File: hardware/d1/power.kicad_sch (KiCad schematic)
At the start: 0 parts

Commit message: New components
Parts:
- added U7: TPS7A2018PDBVR, JLCImport:TPS7A2018PDBVR, symbol JLCImport:TPS7A2018PDBVR
- added U8: TPS7A2033PDBVR, JLCImport:TPS7A2033PDBVR, symbol JLCImport:TPS7A2033PDBVR
- added U9: TPS560430XFDBVR, JLCImport:TPS560430XFDBVR, symbol JLCImport:TPS560430XFDBVR
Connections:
- new net +3V8: U8.1 (IN)
- new net GND: U8.2 (GND)
- no-connect marks 0 -> 1

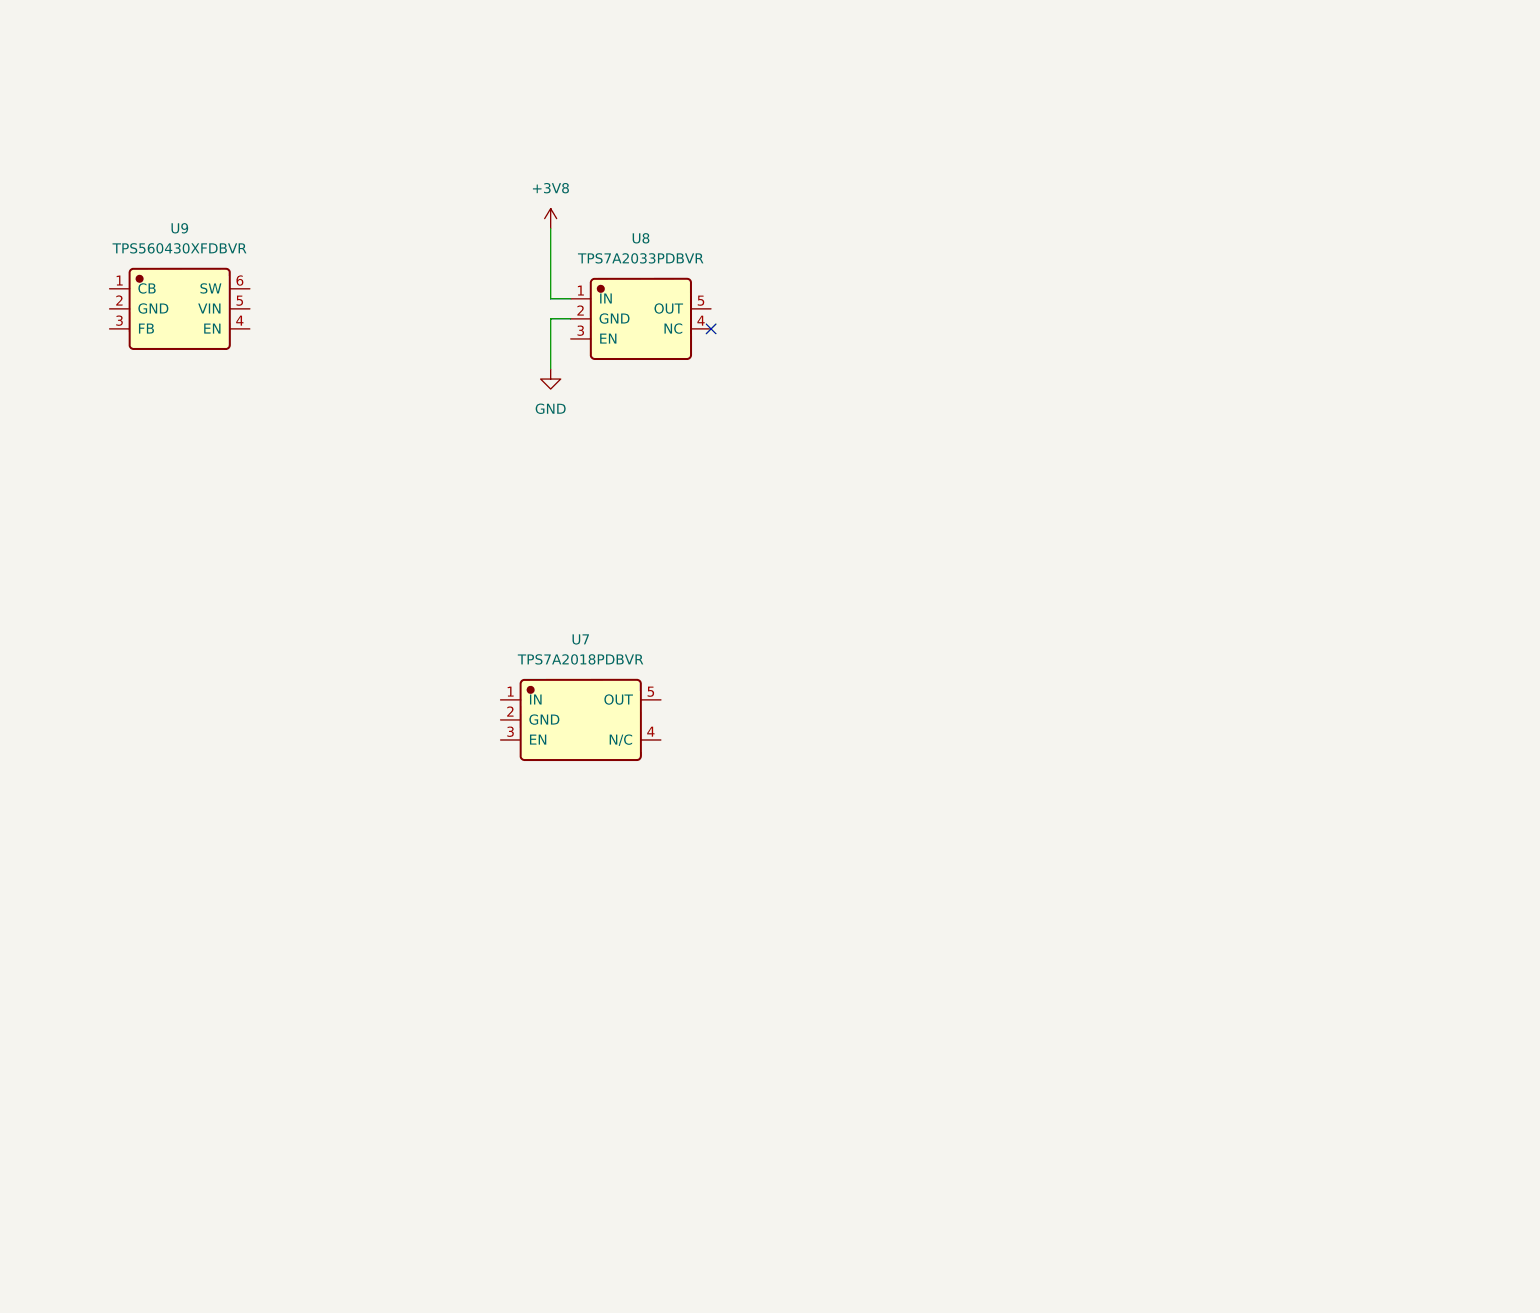
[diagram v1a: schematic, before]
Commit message: Change uart pins, add components
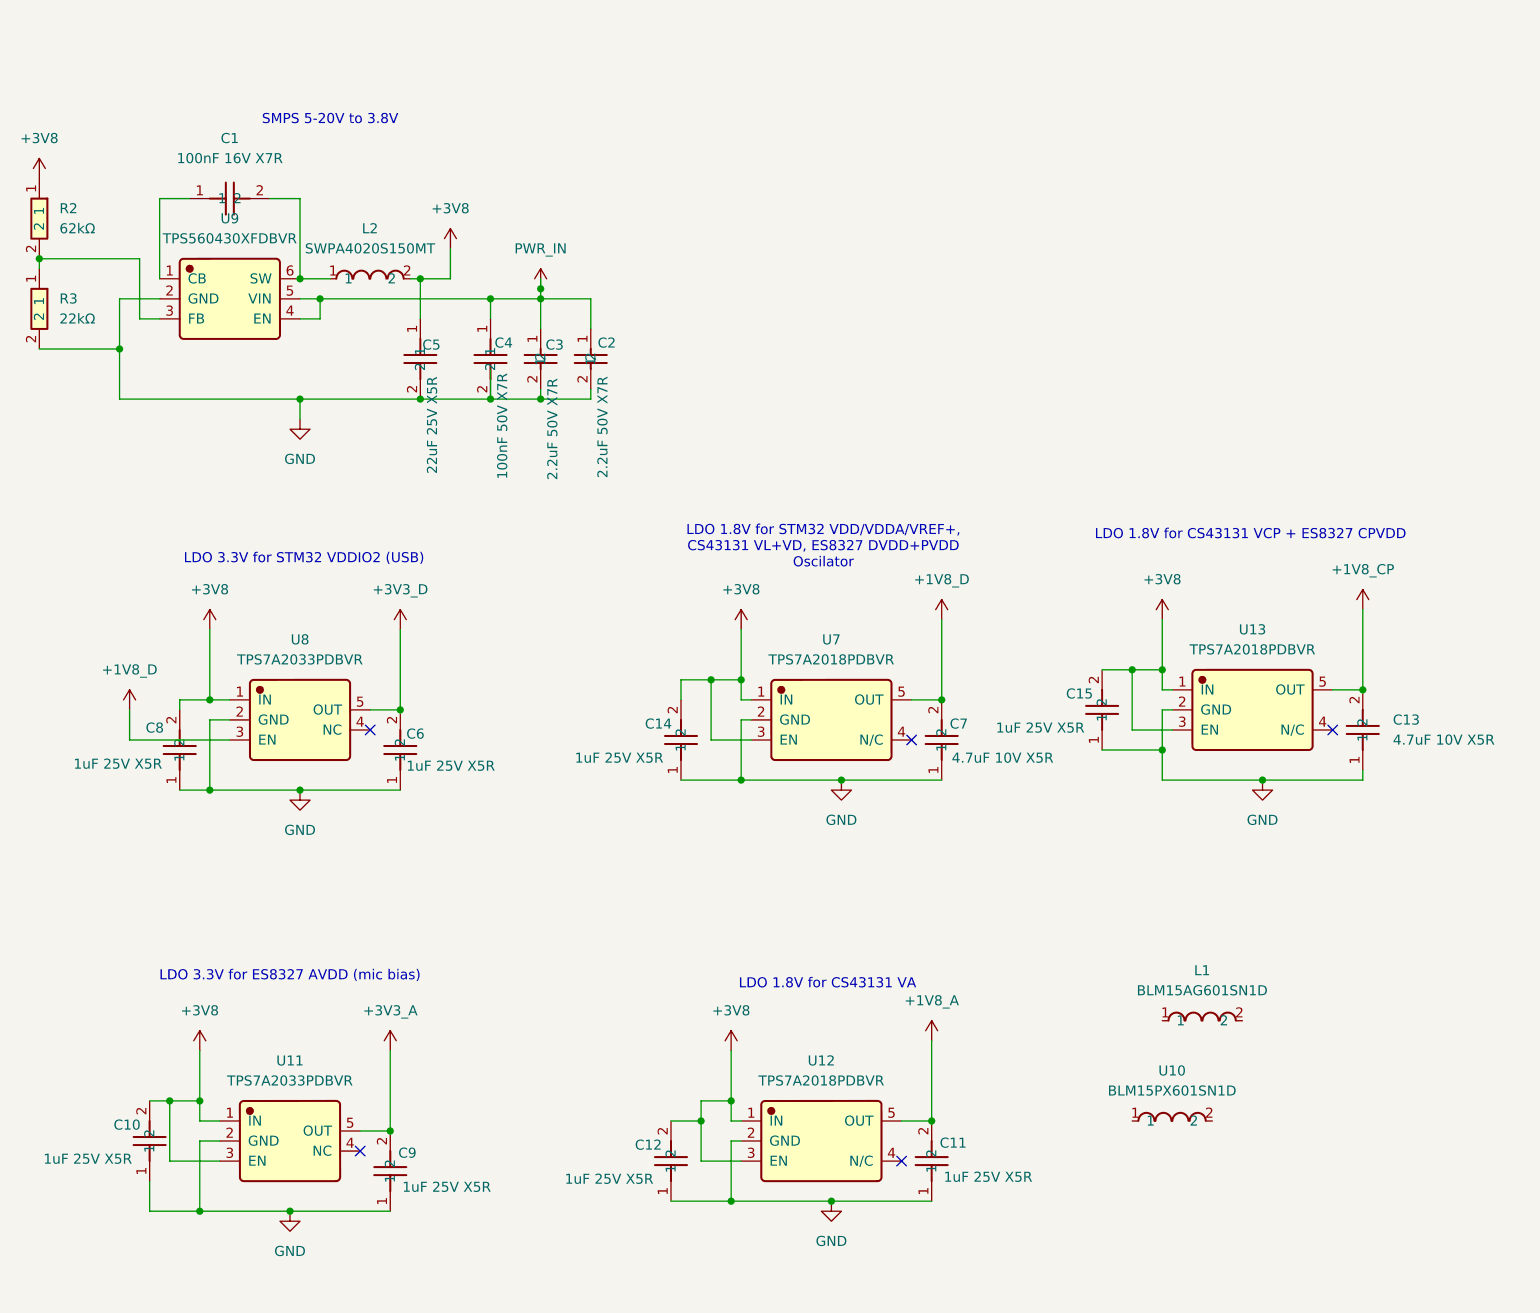
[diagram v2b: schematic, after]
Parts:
- added C1: 100nF 16V X7R, JLCImport:CL05B104KO5NNNC, symbol JLCImport:CL05B104KO5NNNC
- added C10, C11, C12, C14, C15, C6, C8, C9: 1uF 25V X5R, JLCImport:CL05A105KA5NQNC, symbol JLCImport:CL05A105KA5NQNC
- added C13, C7: 4.7uF 10V X5R, JLCImport:CL05A475MP5NRNC, symbol JLCImport:CL05A475MP5NRNC
- added C2, C3: 2.2uF 50V X7R, JLCImport:CC0805KKX7R9BB225, symbol JLCImport:CC0805KKX7R9BB225
- added C4: 100nF 50V X7R, JLCImport:CL05B104KB54PNC, symbol JLCImport:CL05B104KB54PNC
- added C5: 22uF 25V X5R, JLCImport:CL21A226MAQNNNE, symbol JLCImport:CL21A226MAQNNNE
- added L1: BLM15AG601SN1D, JLCImport:BLM15AG601SN1D, symbol JLCImport:BLM15AG601SN1D
- added L2: SWPA4020S150MT, JLCImport:SWPA4020S150MT, symbol JLCImport:SWPA4020S150MT
- added R2: 62kΩ, JLCImport:0402WGF6202TCE, symbol JLCImport:0402WGF6202TCE
- added R3: 22kΩ, JLCImport:0402WGF2202TCE, symbol JLCImport:0402WGF2202TCE
- added U10: BLM15PX601SN1D, JLCImport:BLM15PX601SN1D, symbol JLCImport:BLM15PX601SN1D
- added U11: TPS7A2033PDBVR, JLCImport:TPS7A2033PDBVR, symbol JLCImport:TPS7A2033PDBVR
- added U12, U13: TPS7A2018PDBVR, JLCImport:TPS7A2018PDBVR, symbol JLCImport:TPS7A2018PDBVR
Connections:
- net +3V8: now also U7.1 (IN), U7.3 (EN), C10.2, C12.2, C14.2, C15.2, C5.1, C8.2, L2.2, R2.1, U11.1 (IN), U11.3 (EN), U12.1 (IN), U12.3 (EN), U13.1 (IN), U13.3 (EN)
- net GND: now also U7.2 (GND), U9.2 (GND), C10.1, C11.1, C12.1, C13.1, C14.1, C15.1, C2.2, C3.2, C4.2, C5.2, C6.1, C7.1, C8.1, C9.1, R3.2, U11.2 (GND), U12.2 (GND), U13.2 (GND)
- net +1V8_D: now reaches U8.3 (EN)
- net +1V8_D: now also U7.5 (OUT), C7.2
- net +3V3_D: now reaches U8.5 (OUT)
- net +3V3_D: now also C6.2
- net at U9.1 (CB): now also C1.1
- net at U9.3 (FB): now also R2.2, R3.1
- net PWR_IN: now reaches U9.4 (EN)
- net PWR_IN: now also U9.5 (VIN), C2.1, C3.1, C4.1
- net at U9.6 (SW): now also C1.2, L2.1
- new net +1V8_A: C11.2, U12.5 (OUT)
- new net +1V8_CP: C13.2, U13.5 (OUT)
- new net +3V3_A: C9.2, U11.5 (OUT)
- no-connect marks 1 -> 5
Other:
- note added: "LDO 1.8V for CS43131 VA"
- note added: "LDO 1.8V for CS43131 VCP + ES8327 CPVDD"
- note added: "LDO 1.8V for STM32 VDD/VDDA/VREF+, CS43131 VL+VD, ES8327 DVDD+PVDD Oscilator"
- note added: "LDO 3.3V for ES8327 AVDD (mic bias)"
- note added: "LDO 3.3V for STM32 VDDIO2 (USB)"
- note added: "SMPS 5-20V to 3.8V"
- moved on the sheet: U7, U8, U9

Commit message: Add new parts
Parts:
- removed L1: BLM15AG601SN1D, JLCImport:BLM15AG601SN1D, symbol JLCImport:BLM15AG601SN1D
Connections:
- net +3V8: now also U10.1; no longer C12.2, U12.1 (IN), U12.3 (EN)
- net at U10.2: now also C12.2, U12.1 (IN), U12.3 (EN)
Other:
- moved on the sheet: U10
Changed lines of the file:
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@@
 	)
 	(junction
-		(at 111.76 152.4)
-		(diameter 0)
-		(color 0 0 0 0)
-	)
-	(junction
 		(at 166.37 97.79)
 		(diameter 0)
@@
 	)
 	(junction
+		(at 111.76 152.4)
+		(diameter 0)
+		(color 0 0 0 0)
+	)
+	(junction
 		(at 113.03 111.76)
 		(diameter 0)
@@
 	(wire
 		(pts
+			(xy 91.44 146.05) (xy 99.06 146.05)
+		)
+		(stroke
+			(width 0)
+			(type default)
+		)
+	)
+	(wire
+		(pts
 			(xy 111.76 165.1) (xy 137.16 165.1)
 		)
@@
 	(wire
 		(pts
+			(xy 109.22 146.05) (xy 111.76 146.05)
+		)
+		(stroke
+			(width 0)
+			(type default)
+		)
+	)
+	(wire
+		(pts
 			(xy 111.76 154.94) (xy 113.03 154.94)
 		)
@@
 	(wire
 		(pts
-			(xy 111.76 146.05) (xy 111.76 152.4)
-		)
-		(stroke
-			(width 0)
-			(type default)
-		)
-	)
-	(wire
-		(pts
 			(xy 137.16 154.94) (xy 133.35 154.94)
 		)
@@
 	(wire
 		(pts
+			(xy 111.76 146.05) (xy 111.76 152.4)
+		)
+		(stroke
+			(width 0)
+			(type default)
+		)
+	)
+	(wire
+		(pts
 			(xy 111.76 152.4) (xy 111.76 154.94)
 		)
@@
 	)
 	(symbol
+		(lib_id "power:+3V8")
+		(at 91.44 146.05 0)
+		(unit 1)
+		(body_style 1)
+		(exclude_from_sim no)
+		(in_bom yes)
+		(on_board yes)
+		(in_pos_files yes)
+		(dnp no)
+		(fields_autoplaced yes)
+		(property "Reference" "#PWR011"
+			(at 91.44 149.86 0)
+			(hide yes)
+			(show_name no)
+			(do_not_autoplace no)
+			(effects
+				(font
+					(size 1.27 1.27)
+				)
+			)
+		)
+		(property "Value" "+3V8"
+			(at 91.44 140.97 0)
+			(show_name no)
+			(do_not_autoplace no)
+			(effects
+				(font
+					(size 1.27 1.27)
+				)
+			)
+		)
+		(property "Footprint" ""
+			(at 91.44 146.05 0)
+			(hide yes)
+			(show_name no)
+			(do_not_autoplace no)
+			(effects
+				(font
+					(size 1.27 1.27)
+				)
+			)
+		)
+		(property "Datasheet" ""
+			(at 91.44 146.05 0)
+			(hide yes)
+			(show_name no)
+			(do_not_autoplace no)
+			(effects
+				(font
+					(size 1.27 1.27)
+				)
+			)
+		)
+		(property "Description" "Power symbol creates a global label with name \"+3V8\""
+			(at 91.44 146.05 0)
+			(hide yes)
+			(show_name no)
+			(do_not_autoplace no)
+			(effects
+				(font
+					(size 1.27 1.27)
+				)
+			)
+		)
+		(pin "1"
+		)
+		(instances
+			(project "DrunkEarPhoneAdapter"
+				(path "/df940915-8af0-46f9-b18a-23d4684ae671/bea21a31-aee1-46f9-b13e-ece764487360"
+					(reference "#PWR011")
+					(unit 1)
+				)
+			)
+		)
+	)
+	(symbol
 		(lib_id "power:+5V")
 		(at 87.63 49.53 0)
@@
 	(symbol
 		(lib_id "JLCImport:BLM15PX601SN1D")
-		(at 167.64 154.94 0)
+		(at 104.14 146.05 0)
 		(unit 1)
 		(body_style 1)
@@
 		(fields_autoplaced yes)
 		(property "Reference" "U10"
-			(at 167.6123 148.59 0)
+			(at 104.1123 139.7 0)
 			(show_name no)
 			(do_not_autoplace no)
@@
 		)
 		(property "Value" "BLM15PX601SN1D"
-			(at 167.6123 151.13 0)
+			(at 104.1123 142.24 0)
 			(show_name no)
 			(do_not_autoplace no)
@@
 		)
 		(property "Footprint" "JLCImport:BLM15PX601SN1D"
-			(at 167.64 154.94 0)
+			(at 104.14 146.05 0)
 			(hide yes)
 			(show_name no)
@@
 		)
 		(property "Datasheet" "https://www.lcsc.com/datasheet/lcsc_datasheet_2304140030_Murata-Electronics-BLM15PX601SN1D_C160977.pdf"
-			(at 167.64 154.94 0)
+			(at 104.14 146.05 0)
 			(hide yes)
 			(show_name no)
@@
 		)
 		(property "Description" "-55℃~+125℃ 1 230mΩ 600Ω@100MHz 900mA ±25% 0402 Ferrite Beads ROHS"
-			(at 167.64 154.94 0)
+			(at 104.14 146.05 0)
 			(hide yes)
 			(show_name no)
@@
 		)
 		(property "LCSC" "C160977"
-			(at 167.64 154.94 0)
+			(at 104.14 146.05 0)
 			(hide yes)
 			(show_name no)
@@
 		)
 		(property "Manufacturer" "Murata Electronics"
-			(at 167.64 154.94 0)
+			(at 104.14 146.05 0)
 			(hide yes)
 			(show_name no)
@@
 		)
 		(property "Manufacturer Part" "BLM15PX601SN1D"
-			(at 167.64 154.94 0)
+			(at 104.14 146.05 0)
 			(hide yes)
 			(show_name no)
@@
 	)
 	(symbol
-		(lib_id "power:+3V8")
-		(at 111.76 146.05 0)
-		(unit 1)
-		(body_style 1)
-		(exclude_from_sim no)
-		(in_bom yes)
-		(on_board yes)
-		(in_pos_files yes)
-		(dnp no)
-		(fields_autoplaced yes)
-		(property "Reference" "#PWR011"
-			(at 111.76 149.86 0)
-			(hide yes)
-			(show_name no)
-			(do_not_autoplace no)
-			(effects
-				(font
-					(size 1.27 1.27)
-				)
-			)
-		)
-		(property "Value" "+3V8"
-			(at 111.76 140.97 0)
-			(show_name no)
-			(do_not_autoplace no)
-			(effects
-				(font
-					(size 1.27 1.27)
-				)
-			)
-		)
-		(property "Footprint" ""
-			(at 111.76 146.05 0)
-			(hide yes)
-			(show_name no)
-			(do_not_autoplace no)
-			(effects
-				(font
-					(size 1.27 1.27)
-				)
-			)
-		)
-		(property "Datasheet" ""
-			(at 111.76 146.05 0)
-			(hide yes)
-			(show_name no)
-			(do_not_autoplace no)
-			(effects
-				(font
-					(size 1.27 1.27)
-				)
-			)
-		)
-		(property "Description" "Power symbol creates a global label with name \"+3V8\""
-			(at 111.76 146.05 0)
-			(hide yes)
-			(show_name no)
-			(do_not_autoplace no)
-			(effects
-				(font
-					(size 1.27 1.27)
-				)
-			)
-		)
-		(pin "1"
-		)
-		(instances
-			(project "DrunkEarPhoneAdapter"
-				(path "/df940915-8af0-46f9-b18a-23d4684ae671/bea21a31-aee1-46f9-b13e-ece764487360"
-					(reference "#PWR011")
-					(unit 1)
-				)
-			)
-		)
-	)
-	(symbol
 		(lib_id "JLCImport:TPS560430XFDBVR")
 		(at 48.26 50.8 0)
@@
 					(unit 1)
 				)
-			)
-		)
-	)
-	(symbol
-		(lib_id "JLCImport:BLM15AG601SN1D")
-		(at 171.45 142.24 0)
-		(unit 1)
-		(body_style 1)
-		(exclude_from_sim no)
-		(in_bom yes)
-		(on_board yes)
-		(in_pos_files yes)
-		(dnp no)
-		(fields_autoplaced yes)
-		(property "Reference" "L1"
-			(at 171.4233 135.89 0)
-			(show_name no)
-			(do_not_autoplace no)
-			(effects
-				(font
-					(size 1.27 1.27)
-				)
-			)
-		)
-		(property "Value" "BLM15AG601SN1D"
-			(at 171.4233 138.43 0)
-			(show_name no)
-			(do_not_autoplace no)
-			(effects
-				(font
-					(size 1.27 1.27)
-				)
-			)
-		)
-		(property "Footprint" "JLCImport:BLM15AG601SN1D"
-			(at 171.45 142.24 0)
-			(hide yes)
-			(show_name no)
-			(do_not_autoplace no)
-			(effects
-				(font
-					(size 1.27 1.27)
-				)
-			)
-		)
-		(property "Datasheet" "https://www.lcsc.com/datasheet/lcsc_datasheet_2304140030_Murata-Electronics-BLM15AG601SN1D_C76884.pdf"
-			(at 171.45 142.24 0)
-			(hide yes)
-			(show_name no)
-			(do_not_autoplace no)
-			(effects
-				(font
-					(size 1.27 1.27)
-				)
-			)
-		)
-		(property "Description" "-55℃~+125℃ 1 300mA 520mΩ 600Ω@100MHz ±25% 0402 Ferrite Beads ROHS"
-			(at 171.45 142.24 0)
-			(hide yes)
-			(show_name no)
-			(do_not_autoplace no)
-			(effects
-				(font
-					(size 1.27 1.27)
-				)
-			)
-		)
-		(property "LCSC" "C76884"
-			(at 171.45 142.24 0)
-			(hide yes)
-			(show_name no)
-			(do_not_autoplace no)
-			(effects
-				(font
-					(size 1.27 1.27)
-				)
-			)
-		)
-		(property "Manufacturer" "Murata Electronics"
-			(at 171.45 142.24 0)
-			(hide yes)
-			(show_name no)
-			(do_not_autoplace no)
-			(effects
-				(font
-					(size 1.27 1.27)
-				)
-			)
-		)
-		(property "Manufacturer Part" "BLM15AG601SN1D"
-			(at 171.45 142.24 0)
-			(hide yes)
-			(show_name no)
-			(do_not_autoplace no)
-			(effects
-				(font
-					(size 1.27 1.27)
-				)
-			)
-		)
-		(pin "1"
-		)
-		(pin "2"
-		)
-		(instances
-			(project "DrunkEarPhoneAdapter"
-				(path "/df940915-8af0-46f9-b18a-23d4684ae671/bea21a31-aee1-46f9-b13e-ece764487360"
-					(reference "L1")
-					(unit 1)
-				)

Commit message: Pre-finalize sch
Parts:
- added C51, C57, C58, C59, C60, C61, C62, C63, C64, C65: 22uF 25V X5R, JLCImport:CL21A226MAQNNNE, symbol JLCImport:CL21A226MAQNNNE
- added D2: B5819WS_C916992, Diode_SMD:D_SOD-323, symbol JLCImport:B5819WS_C916992
- added R16: 33Ω 0805, Resistor_SMD:R_0805_2012Metric, symbol JLCImport:0805W8F330JT5E
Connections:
- net GND: now also C51.1, C57.1, C58.1, C59.1, C60.1, C61.1, C62.1, C63.1, C64.1
- net PWR_IN: now also D2.1 (K), R16.1
- new net: C51.2, C57.2, C58.2, C59.2, C60.2, C61.2, C62.2, C63.2, C64.2, C65.2, D2.2 (A), R16.2
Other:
- note added: "Discharge diode"
- note added: "LDO 1.8V for STM32 VDD/VDDA/VREF+, CS43131 VL+VD, ES8327 PVDD Oscilator"
- note added: "LDO 3.3V for STM32 VDDIO2 (USB) ES8327 DVDD, TCPP VCC_VCONN"
- note added: "To hold enegy on role swith events"
- note removed: "LDO 1.8V for STM32 VDD/VDDA/VREF+, CS43131 VL+VD, ES8327 DVDD+PVDD Oscilator"
- note removed: "LDO 3.3V for STM32 VDDIO2 (USB)"

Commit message: Fixes
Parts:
- removed C4: 100nF 50V X7R, JLCImport:CL05B104KB54PNC, symbol JLCImport:CL05B104KB54PNC
- removed C9: 1uF 25V X5R, JLCImport:CL05A105KA5NQNC, symbol JLCImport:CL05A105KA5NQNC
- removed D2: B5819WS_C916992, Diode_SMD:D_SOD-323, symbol JLCImport:B5819WS_C916992
- added C4: 2.2uF 50V X7R, JLCImport:CC0805KKX7R9BB225, symbol JLCImport:CC0805KKX7R9BB225
- added C84, C85: 22uF 25V X5R, JLCImport:CL21A226MAQNNNE, symbol JLCImport:CL21A226MAQNNNE
- added C86: 100nF 50V X7R, Capacitor_SMD:C_0402_1005Metric, symbol JLCImport:CC0402KRX7R9BB104
- added D2: PMEG4010CEH_115, Diode_SMD:D_SOD-123F, symbol JLCImport:PMEG4010CEH_115
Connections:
- net +3V3_A: now also C4.1
- net GND: now also C4.2, C84.1, C85.1, C86.1
- net PWR_IN: now also C86.2, D2.1 (K)
- net at C51.2, C57.2, C58.2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: now also C84.2, C85.2, D2.2 (A)
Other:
- note added: "To hold enegy on role switch events"
- note removed: "To hold enegy on role swith events"

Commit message: Fixes
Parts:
- removed R16: 33Ω 0805, Resistor_SMD:R_0805_2012Metric, symbol JLCImport:0805W8F330JT5E
- added R1: 100Ω 1206, Resistor_SMD:R_1206_3216Metric, symbol JLCImport:SR1206JR-7W100RL
- added TP1: 3V3_D, TestPoint:TestPoint_Pad_1.0x1.0mm, symbol Connector:TestPoint
- added TP2: 1V8_D, TestPoint:TestPoint_Pad_1.0x1.0mm, symbol Connector:TestPoint
- added TP3: 1V8_CP, TestPoint:TestPoint_Pad_1.0x1.0mm, symbol Connector:TestPoint
- added TP4: 1V8_VA, TestPoint:TestPoint_Pad_1.0x1.0mm, symbol Connector:TestPoint
- added TP5: 3V3_VA, TestPoint:TestPoint_Pad_1.0x1.0mm, symbol Connector:TestPoint
- added TP6: 3V8, TestPoint:TestPoint_Pad_1.0x1.0mm, symbol Connector:TestPoint
- added TP7: PWR_IN, TestPoint:TestPoint_Pad_1.0x1.0mm, symbol Connector:TestPoint
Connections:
- net +1V8_A: now also TP4.1
- net +1V8_CP: now also TP3.1
- net +1V8_D: now also TP2.1; no longer U8.3 (EN)
- net +3V3_A: now also TP5.1
- net +3V3_D: now also TP1.1
- net +3V8: now also U8.3 (EN), TP6.1
- net GND: now also C65.1
- net PWR_IN: now also R1.1, TP7.1
- net at C51.2, C57.2, C58.2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: now also R1.2
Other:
- note added: "LDO 1.8V for CS43131 VL+VD, Oscilators, shifters"
- note added: "LDO 3.3V for STM32, ES8327, shifters"
- note removed: "LDO 1.8V for STM32 VDD/VDDA/VREF+, CS43131 VL+VD, ES8327 PVDD Oscilator"
- note removed: "LDO 3.3V for STM32 VDDIO2 (USB) ES8327 DVDD, TCPP VCC_VCONN"
- moved on the sheet: D2

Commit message: Fixes
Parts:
- removed C2, C3: 2.2uF 50V X7R, JLCImport:CC0805KKX7R9BB225, symbol JLCImport:CC0805KKX7R9BB225
- removed C51, C57, C58, C59, C60, C61, C62, C63, C64, C65, C84, C85: 22uF 25V X5R, JLCImport:CL21A226MAQNNNE, symbol JLCImport:CL21A226MAQNNNE
- removed C7: 4.7uF 10V X5R, JLCImport:CL05A475MP5NRNC, symbol JLCImport:CL05A475MP5NRNC
- added C3: 4.7uF 10V X5R, Capacitor_SMD:C_0603_1608Metric, symbol JLCImport:CL10A475KP8NNNC
- added C51, C57, C58, C59, C60, C61, C62, C63, C9: 47uF 25V X5R, Capacitor_SMD:C_1206_3216Metric, symbol JLCImport:C3216X5R1E476MTJ00E
- added C67, C68: 2.2uF 50V X7R, Capacitor_SMD:C_1206_3216Metric, symbol JLCImport:CL31B225KBHNNNE
- added C75: 22uF 25V X5R, JLCImport:CL21A226MAQNNNE, symbol JLCImport:CL21A226MAQNNNE
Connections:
- net +1V8_D: now also C3.2
- net +3V8: now also C75.1
- net GND: now also C3.1, C51.1, C57.1, C58.1, C59.1, C60.1, C61.1, C62.1, C63.1, C67.1, C68.1, C75.2, C9.1
- net PWR_IN: now also C67.2, C68.2
- net at D2.2 (A), R1.2: now also C51.2, C57.2, C58.2, C59.2, C60.2, C61.2, C62.2, C63.2, C9.2
